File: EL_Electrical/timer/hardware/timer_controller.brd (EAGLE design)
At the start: 44 x 36 mm, 20 parts, among them IC2 TC4S584F, IC3 TC4S584F, IC4 LM555D, Q1 BSS138, T1 2N2369

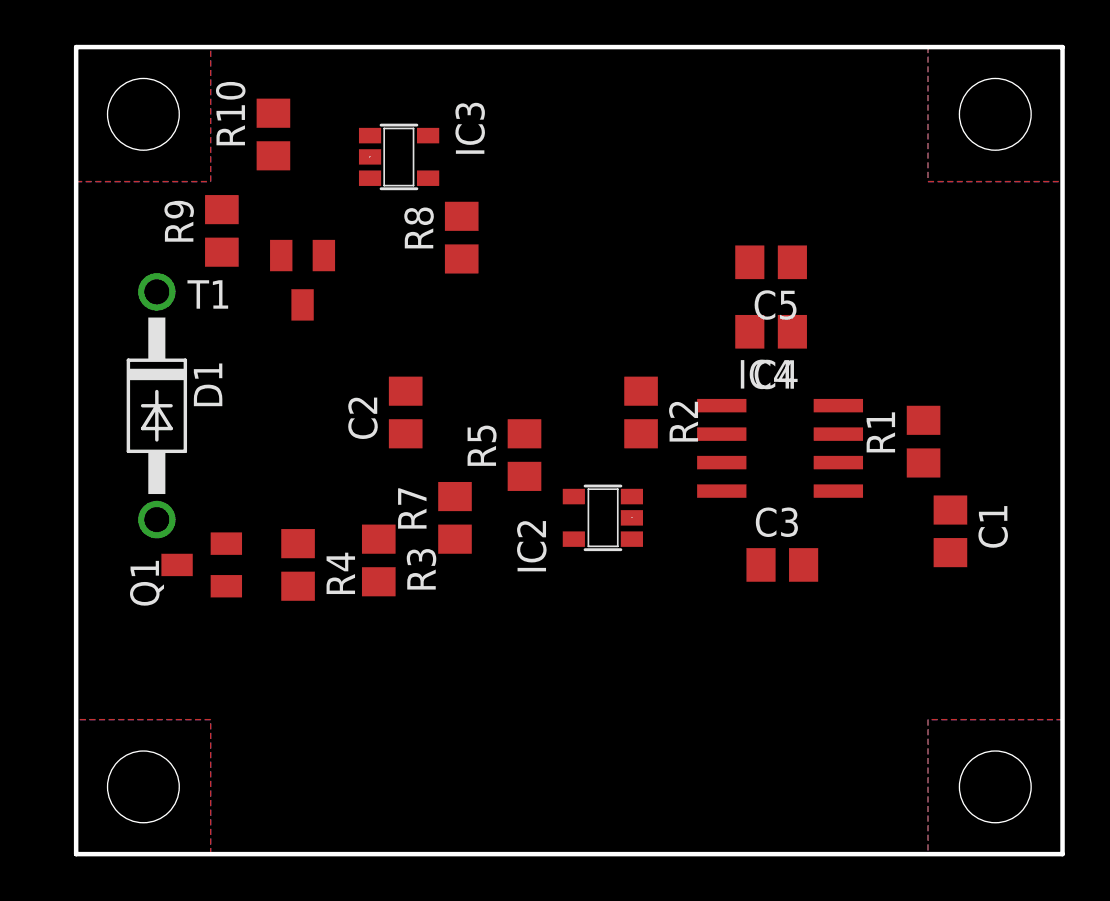
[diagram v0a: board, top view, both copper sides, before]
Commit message: Update sch and PCB (Timer Controller)
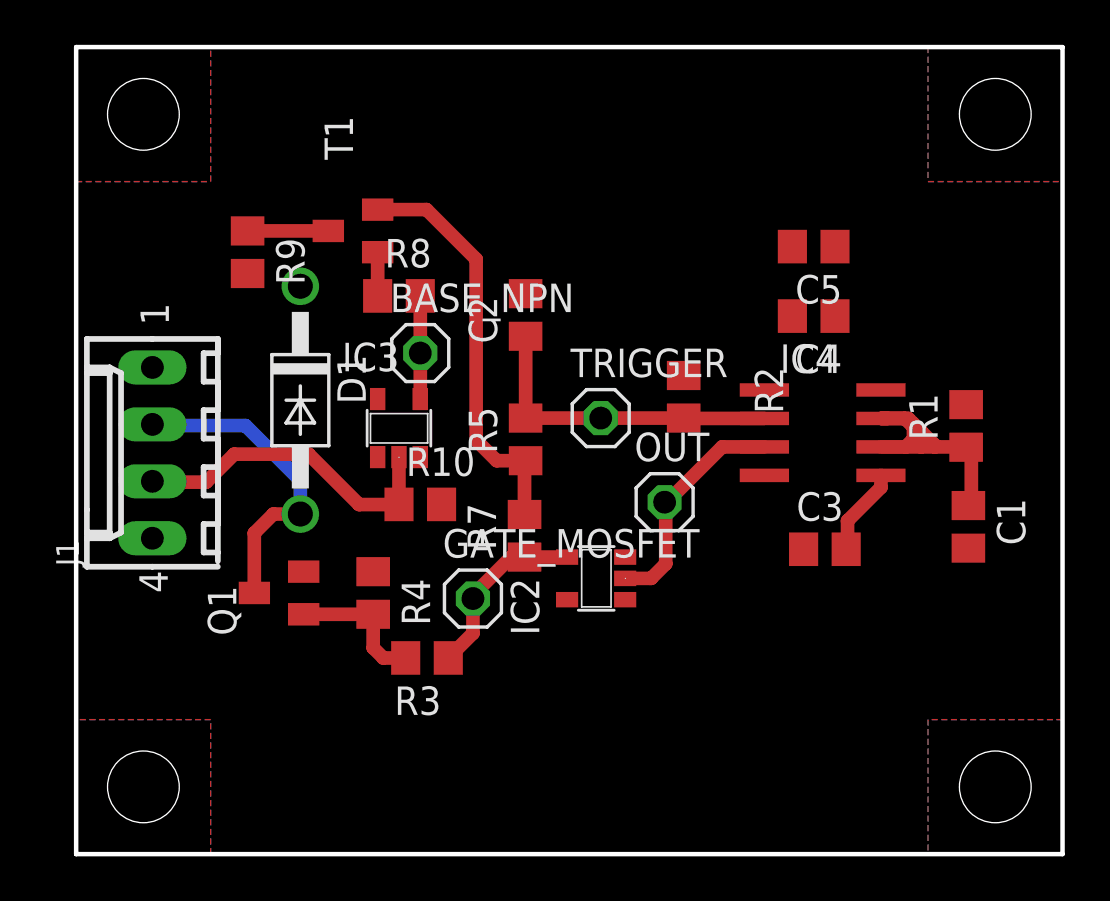
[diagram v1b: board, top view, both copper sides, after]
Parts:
- added BASE_NPN: BASE_NPN, pinhead:1X01
- added GATE_MOSFET: GATE_MOSFET, pinhead:1X01
- added J1: 22-27-2041-04, con-molex:6410-04
- added OUT: OUT, pinhead:1X01
- added TRIGGER: TRIGGER, pinhead:1X01
- C2: value 200µF -> 22µF
- R2: value 1.8k -> 18k
- R5: value 1.2k -> 12k
- moved R10 17.8 mm to (15.3, 15.6), turned to 0 degrees
- moved IC3 12.1 mm to (14.4, 19.0), turned to 0 degrees
- moved C2 6.90 mm to (20.1, 24.1)
- moved D1 6.40 mm to (10.0, 20.2)
- moved R3 4.85 mm to (15.7, 8.75), turned to 180 degrees
- moved R8 3.82 mm to (14.4, 24.9), turned to 0 degrees
- moved Q1 3.67 mm to (9.05, 11.7)
- moved R4 3.58 mm to (13.2, 11.7)
- moved R7 3.20 mm to (20.0, 14.2)
- moved T1 3.15 mm to (12.3, 27.8), turned to 90 degrees
- moved IC2 2.72 mm to (23.2, 12.3)
- moved R1 2.02 mm to (39.7, 19.1)
- moved R2 2.02 mm to (27.1, 20.4)
- moved C5 2.02 mm to (32.9, 27.1)
- moved C3 2.02 mm to (33.4, 13.6)
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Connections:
- removed net N$19: R5.1, R7.2, T1.3
- removed net N$21: IC2.4, R3.1, R7.1
- removed net N$23: C4.2, C5.2
- removed net N$24: IC2.2, IC4.3
- removed net N$25: IC3.4, R8.2
- removed net VCC: IC2.5, IC3.5
- new net BASE_NPN: BASE_NPN.1, IC3.4, R8.2
- new net GATE_MOSFET: GATE_MOSFET.1, IC2.4, R3.1, R7.1
- new net N$2: R9.1, T1.3
- new net OUT: IC2.2, IC4.3, OUT.1
- net +12V: now also IC2.5, IC3.5, J1.1
- net BP_START: now also J1.3
- net GND: now also C4.2, C5.2, J1.4
- net N$26: now also R5.1, R7.2; no longer R9.1
- net RELAIS_INJECTEUR: now also J1.2
- net TRIGGER: now also TRIGGER.1
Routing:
- net N$26: track 0.00 -> 18.4 mm
- net BP_START: track 0.00 -> 14.6 mm
- net TRIGGER: track 0.00 -> 14.3 mm
- net RELAIS_INJECTEUR: track 0.00 -> 14.2 mm
- net N$17: track 0.00 -> 13.8 mm
- net OUT: track 0.00 -> 10.3 mm
- net GATE_MOSFET: track 0.00 -> 8.16 mm
- net N$1: track 0.00 -> 6.24 mm
- net BASE_NPN: track 0.00 -> 4.60 mm
- net N$9: track 0.00 -> 3.92 mm
- net N$2: track 0.00 -> 3.60 mm
- net N$27: track 0.00 -> 1.95 mm
- net +12V: track 0.00 -> 0.87 mm
- added copper zone on layer 16, net +12V
- removed copper zone on layer 16, net +5V

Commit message: Update holes and text
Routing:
- net +12V: track 0.87 -> 20.1 mm, vias 0 -> 4
- net N$17: track 13.8 -> 13.2 mm
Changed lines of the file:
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@@
 <contactref element="C4" pad="2"/>
 <contactref element="C5" pad="2"/>
-<wire x1="24.49" y1="13.25" x2="27.1" y2="21.35" width="0" layer="19" extent="1-1"/>
 </signal>
 <signal name="+12V">
@@
 <contactref element="IC3" pad="5"/>
 <contactref element="IC2" pad="5"/>
-<wire x1="33.984" y1="24.2136" x2="33.85" y2="24" width="0.6096" layer="1"/>
-<wire x1="33.984" y1="26.7624" x2="33.85" y2="27.1" width="0.6096" layer="1"/>
-<wire x1="33.984" y1="23.7888" x2="33.85" y2="24" width="0.6096" layer="1"/>
 <polygon width="0.2" layer="16" isolate="0.2">
 <vertex x="6" y="36"/>
@@
 <vertex x="6" y="30"/>
 </polygon>
-<wire x1="33.984" y1="24.2136" x2="33.984" y2="26.7624" width="0" layer="19" extent="1-1"/>
-<wire x1="35.9" y1="20.705" x2="33.984" y2="23.7888" width="0" layer="19" extent="1-1"/>
-<wire x1="39.7" y1="20.05" x2="35.9" y2="20.705" width="0" layer="19" extent="1-1"/>
-<wire x1="30.7" y1="16.895" x2="35.9" y2="20.705" width="0" layer="19" extent="1-1"/>
-<wire x1="21.9" y1="11.35" x2="30.7" y2="16.895" width="0" layer="19" extent="1-1"/>
-<wire x1="16.3" y1="15.6" x2="21.9" y2="11.35" width="0" layer="19" extent="1-1"/>
-<wire x1="13.45" y1="20.3" x2="16.3" y2="15.6" width="0" layer="19" extent="1-1"/>
-<wire x1="10" y1="25.33" x2="13.45" y2="20.3" width="0" layer="19" extent="1-1"/>
-<wire x1="7.65" y1="25.9" x2="10" y2="25.33" width="0" layer="19" extent="1-1"/>
-<wire x1="3.4" y1="21.71" x2="7.65" y2="25.9" width="0" layer="19" extent="1-1"/>
+<wire x1="21.9" y1="11.35" x2="20.6" y2="11.35" width="0.6096" layer="1"/>
+<via x="20.6" y="11.35" extent="1-16" drill="0.35"/>
+<wire x1="33.85" y1="27.1" x2="33.85" y2="28.75" width="0.6096" layer="1"/>
+<via x="33.85" y="28.75" extent="1-16" drill="0.35"/>
+<wire x1="39.7" y1="20.05" x2="38.4" y2="20.05" width="0.6096" layer="1"/>
+<wire x1="37.745" y1="20.705" x2="35.9" y2="20.705" width="0.6096" layer="1"/>
+<wire x1="38.4" y1="20.05" x2="37.745" y2="20.705" width="0.6096" layer="1"/>
+<wire x1="33.85" y1="27.1" x2="33.85" y2="24" width="0.6096" layer="1"/>
+<wire x1="33.85" y1="24" x2="33.85" y2="21.15" width="0.6096" layer="1"/>
+<wire x1="33.85" y1="21.15" x2="34.3" y2="20.7" width="0.6096" layer="1"/>
+<wire x1="34.3" y1="20.7" x2="35.895" y2="20.7" width="0.6096" layer="1"/>
+<wire x1="35.895" y1="20.7" x2="35.9" y2="20.705" width="0.6096" layer="1"/>
+<wire x1="7.65" y1="25.9" x2="9.43" y2="25.9" width="0.6096" layer="1"/>
+<wire x1="9.43" y1="25.9" x2="10" y2="25.33" width="0.6096" layer="1"/>
+<wire x1="16.3" y1="15.6" x2="17.6" y2="15.6" width="0.6096" layer="1"/>
+<via x="17.6" y="15.6" extent="1-16" drill="0.35"/>
+<via x="12.4" y="20.3" extent="1-16" drill="0.35"/>
+<wire x1="13.45" y1="20.3" x2="12.4" y2="20.3" width="0.6096" layer="1"/>
+<wire x1="35.9" y1="20.705" x2="30.7" y2="16.895" width="0" layer="19" extent="1-1"/>
 </signal>
 <signal name="N$9">
@@
 <contactref element="IC4" pad="5"/>
 <wire x1="34.4088" y1="14.868" x2="34.4088" y2="14.0184" width="0.6096" layer="1"/>
-<wire x1="34.4088" y1="14.0184" x2="34.35" y2="13.6" width="0.6096" layer="1"/>
 <wire x1="35.9" y1="16.895" x2="35.9" y2="16.3592" width="0.6096" layer="1"/>
 <wire x1="35.9" y1="16.3592" x2="34.4088" y2="14.868" width="0.6096" layer="1"/>
+<wire x1="34.4088" y1="14.0184" x2="34.35" y2="13.6" width="0" layer="19" extent="1-1"/>
 </signal>
 <signal name="N$17">
@@
 <wire x1="39.685" y1="18.165" x2="39.7" y2="18.15" width="0.6096" layer="1"/>
 <wire x1="39.9312" y1="17.8416" x2="39.9312" y2="15.7176" width="0.6096" layer="1"/>
-<wire x1="39.9312" y1="15.7176" x2="39.8" y2="15.55" width="0.6096" layer="1"/>
-<wire x1="39.9312" y1="17.8416" x2="39.7" y2="18.15" width="0.6096" layer="1"/>
 <wire x1="36.19395" y1="19.435" x2="35.9" y2="19.435" width="0.6096" layer="1"/>
 <wire x1="35.9" y1="19.435" x2="37.115" y2="19.435" width="0.6096" layer="1"/>
@@
 <wire x1="37.35" y1="19.2" x2="37.35" y2="18.515" width="0.6096" layer="1"/>
 <wire x1="37.35" y1="18.515" x2="37" y2="18.165" width="0.6096" layer="1"/>
+<wire x1="39.9312" y1="15.7176" x2="39.8" y2="15.55" width="0" layer="19" extent="1-1"/>
+<wire x1="39.7" y1="18.15" x2="39.9312" y2="17.8416" width="0" layer="19" extent="1-1"/>
 </signal>
 <signal name="TRIGGER">
@@
 <contactref element="D1" pad="A"/>
 <contactref element="J1" pad="2"/>
-<wire x1="7.9464" y1="14.3184" x2="7.9464" y2="11.653265625" width="0.6096" layer="1"/>
-<wire x1="8.798" y1="15.17" x2="7.9464" y2="14.3184" width="0.6096" layer="1"/>
-<wire x1="7.9464" y1="11.653265625" x2="7.95" y2="11.65" width="0.6096" layer="1"/>
-<wire x1="10" y1="15.17" x2="8.798" y2="15.17" width="0.6096" layer="1"/>
-<wire x1="7.554" y1="19.116" x2="3.8232" y2="19.116" width="0.6096" layer="16"/>
-<wire x1="10" y1="16.67" x2="7.554" y2="19.116" width="0.6096" layer="16"/>
-<wire x1="3.8232" y1="19.116" x2="3.4" y2="19.17" width="0.6096" layer="16"/>
-<wire x1="10" y1="15.17" x2="10" y2="16.67" width="0.6096" layer="16"/>
+<wire x1="8.798" y1="15.17" x2="10" y2="15.17" width="0.6096" layer="1"/>
+<wire x1="10" y1="16.67" x2="10" y2="15.17" width="0.6096" layer="16"/>
+<wire x1="3.4" y1="19.17" x2="7.5" y2="19.17" width="0.6096" layer="16"/>
+<wire x1="7.5" y1="19.17" x2="10" y2="16.67" width="0.6096" layer="16"/>
+<wire x1="7.95" y1="11.65" x2="7.95" y2="14.322" width="0.6096" layer="1"/>
+<wire x1="7.95" y1="14.322" x2="8.798" y2="15.17" width="0.6096" layer="1"/>
 </signal>
 <signal name="N$26">

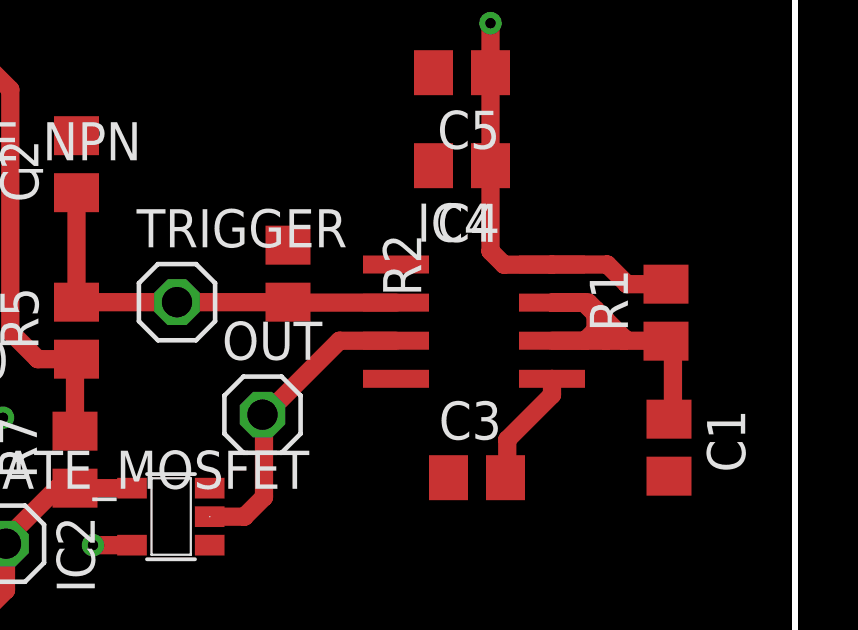
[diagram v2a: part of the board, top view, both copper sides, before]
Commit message: Update timer_controller
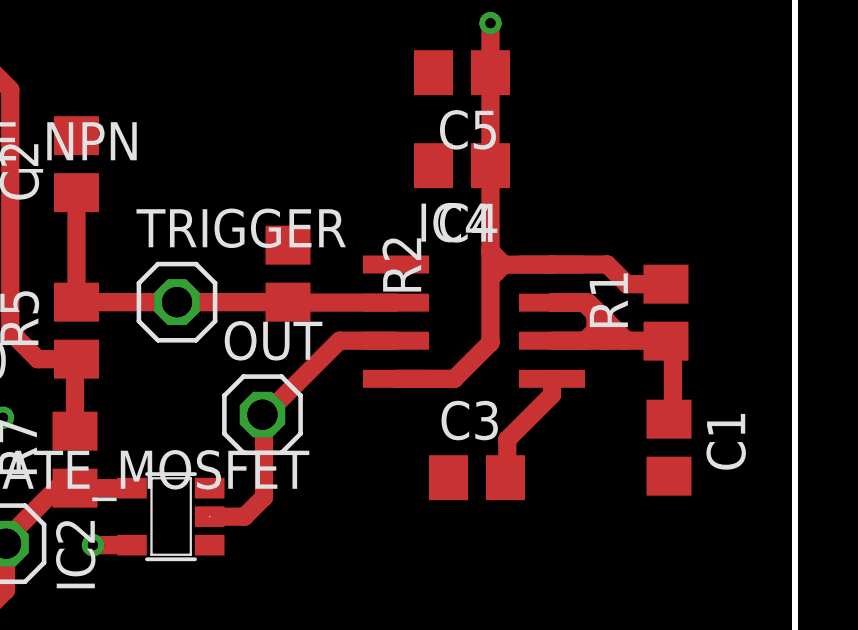
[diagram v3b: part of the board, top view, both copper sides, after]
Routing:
- net +12V: track 20.1 -> 27.4 mm
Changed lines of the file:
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@@
 <via x="12.4" y="20.3" extent="1-16" drill="0.35"/>
 <wire x1="13.45" y1="20.3" x2="12.4" y2="20.3" width="0.6096" layer="1"/>
-<wire x1="35.9" y1="20.705" x2="30.7" y2="16.895" width="0" layer="19" extent="1-1"/>
+<wire x1="32.645" y1="16.895" x2="30.7" y2="16.895" width="0.6096" layer="1"/>
+<wire x1="33.9" y1="20.3" x2="34.3" y2="20.7" width="0.6096" layer="1"/>
+<wire x1="33.85" y1="18.1" x2="32.645" y2="16.895" width="0.6096" layer="1"/>
+<wire x1="33.85" y1="21.15" x2="33.85" y2="18.1" width="0.6096" layer="1"/>
 </signal>
 <signal name="N$9">
